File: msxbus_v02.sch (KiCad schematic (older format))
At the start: 4 parts, among them J1 RPi_GPIO, P1 MSX_SLOT, P2 MSX_SLOT, U1 CPLD

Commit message: PCB update
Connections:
- net CLOCK: now also U1.46 (VCC); no longer U1.48 (G27)
- net D4: now also U1.49 (G28)
- net D5: now also U1.50 (G29)
- net D6: now also U1.47 (G26); no longer U1.49 (G28)
- net D7: now also U1.48 (G27); no longer U1.50 (G29)
- net GND: now also U1.1 (GND), U1.2 (GND), U1.44 (GND)
- net RG00: now also U1.20 (G95); no longer U1.23 (G98)
- net RG01: now also U1.21 (G96); no longer U1.24 (G99)
- net RG02: now also U1.3 (G74); no longer U1.6 (G77)
- net RG03: now also U1.4 (G75); no longer U1.7 (G78)
- net RG04: now also U1.5 (G76); no longer U1.34 (G12), U1.8 (G81)
- net RG05: now also U1.22 (G97); no longer U1.25 (G100)
- net RG06: now also U1.23 (G98); no longer U1.26 (G1)
- net RG07: now also U1.19 (G92); no longer U1.22 (G97)
- net RG08: now also U1.18 (G91); no longer U1.21 (G96)
- net RG09: now also U1.15 (G88); no longer U1.18 (G91)
- net RG10: now also U1.14 (G87); no longer U1.17 (G90)
- net RG11: now also U1.17 (G90); no longer U1.20 (G95)
- net RG12: now also U1.24 (G99); no longer U1.27 (G2)
- net RG13: now also U1.25 (G100); no longer U1.28 (G3)
- net RG14: now also U1.6 (G77); no longer U1.9 (G82)
- net RG15: now also U1.7 (G78); no longer U1.10 (G83)
- net RG16: now also U1.27 (G2); no longer U1.30 (G5)
- net RG17: now also U1.8 (G81); no longer U1.11 (G84)
- net RG18: now also U1.9 (G82); no longer U1.12 (G85)
- net RG19: now also U1.26 (G1); no longer U1.29 (G4)
- net RG20: now also U1.29 (G4); no longer U1.32 (G7)
- net RG21: now also U1.30 (G5); no longer U1.33 (G8)
- net RG22: now also U1.11 (G84); no longer U1.14 (G87)
- net RG23: now also U1.12 (G85); no longer U1.15 (G88)
- net RG24: now also U1.13 (G86); no longer U1.16 (G89)
- net RG25: now also U1.16 (G89); no longer U1.19 (G92)
- net RG26: now also U1.28 (G3); no longer U1.31 (G6)
- net RG27: now also U1.10 (G83); no longer U1.13 (G86)
- net SLTSL1: no longer P2.4 (P4)
- net SLTSL2: now also P2.4 (P4)
- net SW1: now also P1.46 (P46), U1.42 (G21); no longer P1.44 (P44), P2.44 (P44), U1.45 (GND)
- net SW2: now also U1.41 (G20); no longer P1.46 (P46), U1.46 (VCC)
- net SWOUT: now also P1.44 (P44), P2.44 (P44), U1.45 (GND); no longer U1.47 (G26)
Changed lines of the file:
@@
 CLOCK
 Text Label 10150 3200 0    60   ~ 0
+SWOUT
+Text Label 10150 3300 0    60   ~ 0
 SW1
-Text Label 10150 3300 0    60   ~ 0
-SW2
 $Comp
 L MSX_SLOT P2
@@
 GND
 Text Label 10150 4050 0    60   ~ 0
-SLTSL1
+SLTSL2
 Text Label 10150 4150 0    60   ~ 0
 RFSH
@@
 CLOCK
 Text Label 10150 6050 0    60   ~ 0
-SW1
+SWOUT
 Text Label 10150 6150 0    60   ~ 0
 SW2
@@
 Text Label 7350 5250 0    60   ~ 0
 D2
-Text Label 7350 5350 0    60   ~ 0
+Text Label 7350 5550 0    60   ~ 0
 D7
-Text Label 7350 5450 0    60   ~ 0
+Text Label 7350 5650 0    60   ~ 0
 D6
-Text Label 7350 5550 0    60   ~ 0
+Text Label 7350 5750 0    60   ~ 0
 CLOCK
-Text Label 7350 5650 0    60   ~ 0
+Text Label 7350 5850 0    60   ~ 0
 SWOUT
-Text Label 7350 5750 0    60   ~ 0
+Text Label 5100 5550 0    60   ~ 0
 SW2
-Text Label 7350 5850 0    60   ~ 0
+Text Label 5100 5650 0    60   ~ 0
 SW1
 Wire Wire Line
@@
 Text Label 3350 3500 0    60   ~ 0
 RG21
-Text Label 5100 4850 0    60   ~ 0
+Text Label 5100 1750 0    60   ~ 0
+RG02
+Text Label 5100 1850 0    60   ~ 0
+RG03
+Text Label 5100 1950 0    60   ~ 0
 RG04
+Text Label 5100 2150 0    60   ~ 0
+RG15
 Text Label 5100 2050 0    60   ~ 0
-RG02
-Text Label 5100 2150 0    60   ~ 0
-RG03
+RG14
+Text Label 5100 2350 0    60   ~ 0
+RG18
 Text Label 5100 2250 0    60   ~ 0
-RG04
-Text Label 5100 2350 0    60   ~ 0
-RG14
+RG17
 Text Label 5100 2450 0    60   ~ 0
-RG15
+RG27
 Text Label 5100 2550 0    60   ~ 0
-RG17
+RG22
 Text Label 5100 2650 0    60   ~ 0
-RG18
+RG23
 Text Label 5100 2750 0    60   ~ 0
-RG27
+RG24
 Text Label 5100 2850 0    60   ~ 0
-RG22
+RG10
 Text Label 5100 2950 0    60   ~ 0
-RG23
+RG09
 Text Label 5100 3050 0    60   ~ 0
-RG24
+RG25
 Text Label 5100 3150 0    60   ~ 0
-RG10
+RG11
 Text Label 5100 3250 0    60   ~ 0
-RG09
+RG08
 Text Label 5100 3350 0    60   ~ 0
-RG25
+RG07
 Text Label 5100 3450 0    60   ~ 0
-RG11
+RG00
 Text Label 5100 3550 0    60   ~ 0
-RG08
+RG01
 Text Label 5100 3650 0    60   ~ 0
-RG07
+RG05
 Text Label 5100 3750 0    60   ~ 0
-RG00
+RG06
 Text Label 5100 3850 0    60   ~ 0
-RG01
+RG12
 Text Label 5100 3950 0    60   ~ 0
-RG05
+RG13
 Text Label 5100 4050 0    60   ~ 0
-RG06
+RG19
 Text Label 5100 4150 0    60   ~ 0
-RG12
+RG16
 Text Label 5100 4250 0    60   ~ 0
-RG13
+RG26
 Text Label 5100 4350 0    60   ~ 0
-RG19
+RG20
 Text Label 5100 4450 0    60   ~ 0
-RG16
-Text Label 5100 4550 0    60   ~ 0
-RG26
-Text Label 5100 4650 0    60   ~ 0
-RG20
-Text Label 5100 4750 0    60   ~ 0
 RG21
 Wire Wire Line
@@
 Text Label 7350 2150 0    60   ~ 0
 CS12
+Text Label 5100 1550 0    60   ~ 0
+GND
+Text Label 5100 1650 0    60   ~ 0
+GND
+Text Label 5100 5850 0    60   ~ 0
+GND
+Text Label 7350 5450 0    60   ~ 0
+D4
+Text Label 7350 5350 0    60   ~ 0
+D5
 $EndSCHEMATC

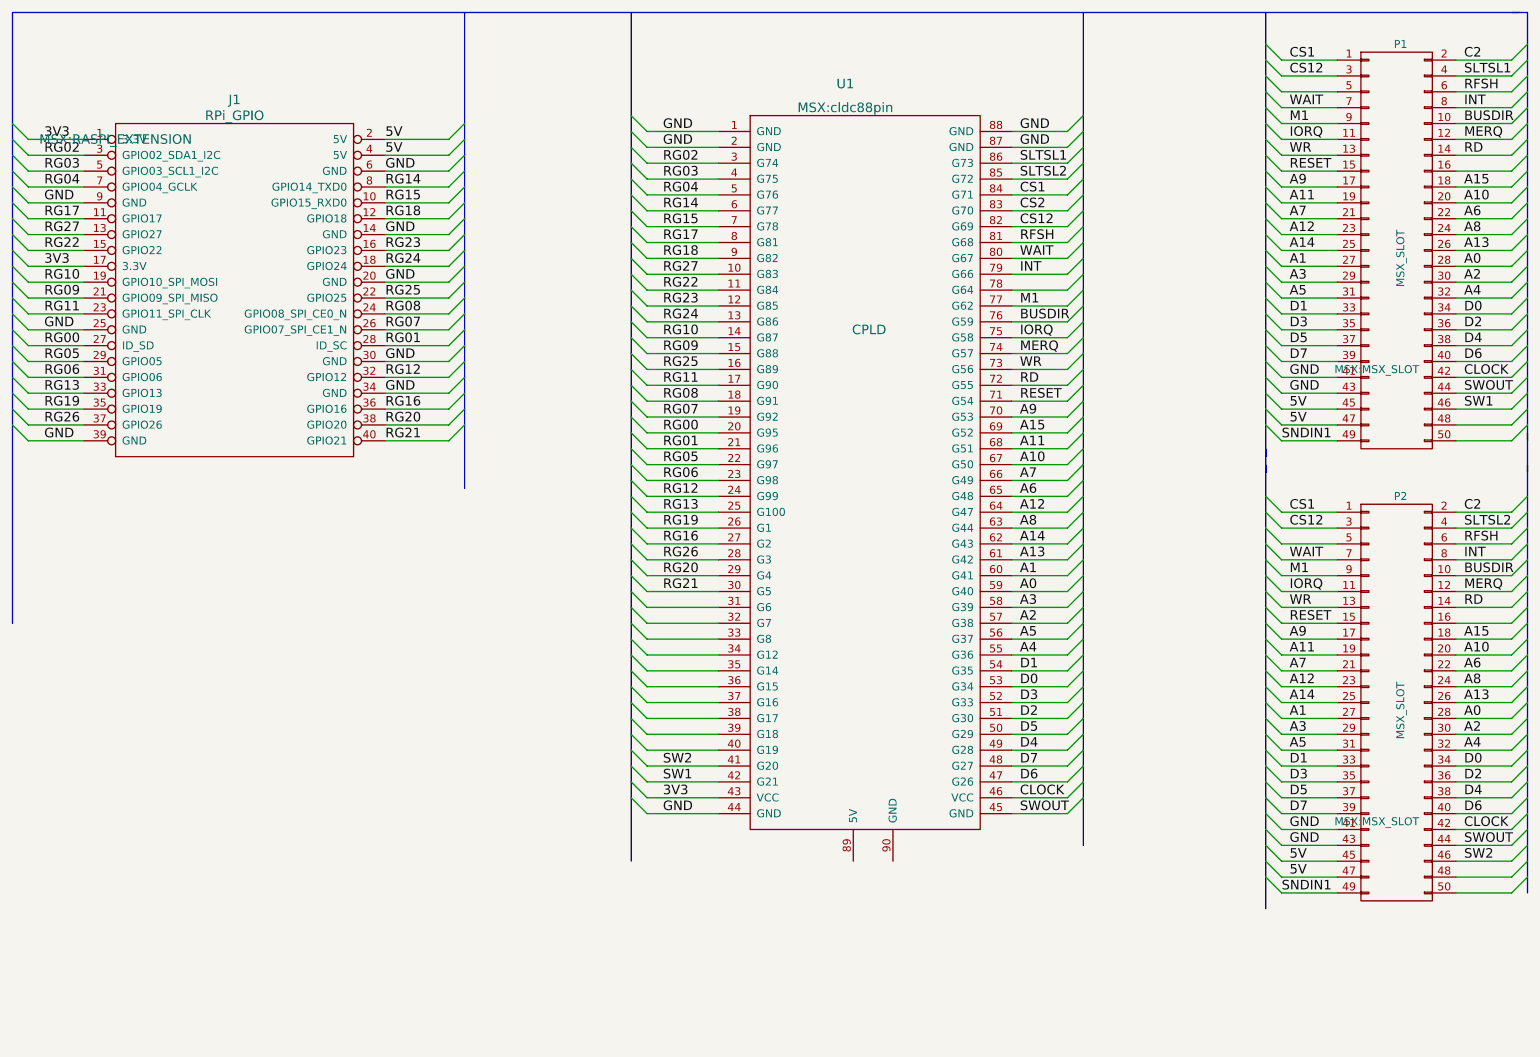
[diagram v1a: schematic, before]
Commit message: update for MSXBUS v0.6
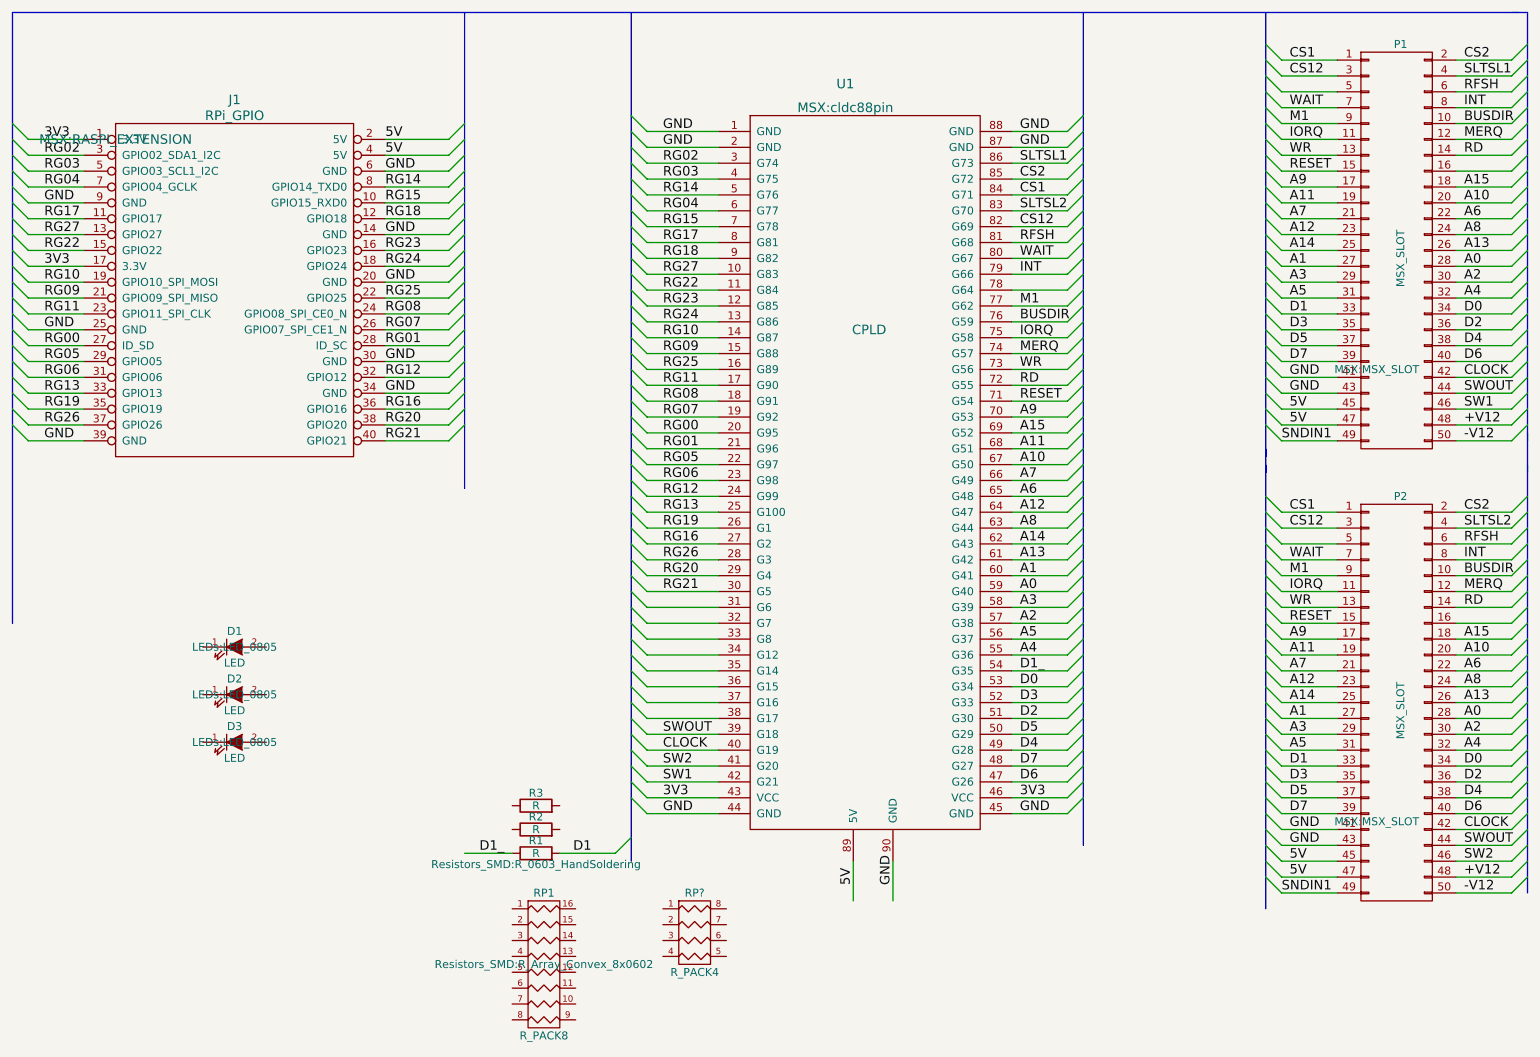
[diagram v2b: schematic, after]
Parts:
- added D1, D2, D3: LED, LEDs:LED_0805, symbol LED
- added R1: R, Resistors_SMD:R_0603_HandSoldering, symbol R
- added R2, R3: R, symbol R
- added RP1: R_PACK8, Resistors_SMD:R_Array_Convex_8x0602, symbol R_PACK8
- added RP?: R_PACK4, ~, symbol R_PACK4
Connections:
- net C2 is gone; now on net CS2: P1.2 (P2), P2.2 (P2)
- net 3V3: now also U1.46 (VCC)
- net 5V: now also U1.89 (5V)
- net CLOCK: now also U1.40 (G19); no longer U1.46 (VCC)
- net CS2: now also U1.85 (G72); no longer U1.83 (G70)
- net D1: now also R1.2; no longer U1.54 (G35)
- net GND: now also U1.45 (GND), U1.90 (GND)
- net RG04: now also U1.6 (G77); no longer U1.5 (G76)
- net RG14: now also U1.5 (G76); no longer U1.6 (G77)
- net SLTSL2: now also U1.83 (G70); no longer U1.85 (G72)
- net SWOUT: now also U1.39 (G18); no longer U1.45 (GND)
- net +V12: now reaches P1.48 (P48)
- net +V12: now also P2.48 (P48)
- net -V12: now reaches P1.50 (P50)
- net -V12: now also P2.50 (P50)
- new net D1_: R1.1, U1.54 (G35)

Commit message: minor update
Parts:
- removed R1: R, Resistors_SMD:R_0603_HandSoldering, symbol R
- removed R2, R3: R, symbol R
- removed RP1: R_PACK8, Resistors_SMD:R_Array_Convex_8x0602, symbol R_PACK8
- RP?: footprint ~ -> Resistors_SMD:R_Array_Convex_4x1206
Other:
- moved on the sheet: RP?
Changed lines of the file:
@@
 	1    0    0    -1
 $EndComp
-$Comp
-L R R1
-U 1 1 5727AC59
-P 4300 6100
-F 0 "R1" V 4380 6100 50  0000 C CNN
-F 1 "R" V 4300 6100 50  0000 C CNN
-F 2 "Resistors_SMD:R_0603_HandSoldering" V 4230 6100 50  0000 C CNN
-F 3 "" H 4300 6100 50  0000 C CNN
-	1    4300 6100
-	0    -1   -1   0
-$EndComp
-$Comp
-L R R2
-U 1 1 5727AD14
-P 4300 5950
-F 0 "R2" V 4380 5950 50  0000 C CNN
-F 1 "R" V 4300 5950 50  0000 C CNN
-F 2 "" V 4230 5950 50  0000 C CNN
-F 3 "" H 4300 5950 50  0000 C CNN
-	1    4300 5950
-	0    -1   -1   0
-$EndComp
-$Comp
-L R R3
-U 1 1 5727AD4D
-P 4300 5800
-F 0 "R3" V 4380 5800 50  0000 C CNN
-F 1 "R" V 4300 5800 50  0000 C CNN
-F 2 "" V 4230 5800 50  0000 C CNN
-F 3 "" H 4300 5800 50  0000 C CNN
-	1    4300 5800
-	0    -1   -1   0
-$EndComp
-Wire Wire Line
-	4150 6100 3850 6100
-Wire Wire Line
-	4450 6100 4800 6100
-Text Label 4100 6100 2    60   ~ 0
-D1_
-Text Label 4650 6100 2    60   ~ 0
-D1
 Entry Wire Line
 	4800 6100 4900 6000
 $Comp
-L R_PACK8 RP1
-U 1 1 5727B68C
-P 4350 6800
-F 0 "RP1" H 4350 7250 50  0000 C CNN
-F 1 "R_PACK8" H 4350 6350 50  0000 C CNN
-F 2 "Resistors_SMD:R_Array_Convex_8x0602" H 4350 6800 50  0000 C CNN
-F 3 "" H 4350 6800 50  0000 C CNN
-	1    4350 6800
+L R_PACK4 RP?
+U 1 1 5727B749
+P 5400 7100
+F 0 "RP?" H 5400 7550 50  0000 C CNN
+F 1 "R_PACK4" H 5400 7050 50  0000 C CNN
+F 2 "Resistors_SMD:R_Array_Convex_4x1206" H 5400 7100 50  0000 C CNN
+F 3 "" H 5400 7100 50  0000 C CNN
+	1    5400 7100
 	1    0    0    -1
 $EndComp
-$Comp
-L R_PACK4 RP?
-U 1 1 5727B749
-P 5300 6800
-F 0 "RP?" H 5300 7250 50  0000 C CNN
-F 1 "R_PACK4" H 5300 6750 50  0000 C CNN
-F 2 "~" H 5300 6800 50  0000 C CNN
-F 3 "" H 5300 6800 50  0000 C CNN
-	1    5300 6800
-	1    0    0    -1
-$EndComp
